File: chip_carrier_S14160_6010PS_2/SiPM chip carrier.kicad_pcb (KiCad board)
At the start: 2 copper layers, 29 x 29 mm, 3 parts, among them J1 Conn_01x10_Socket, J2 Conn_01x10_Socket

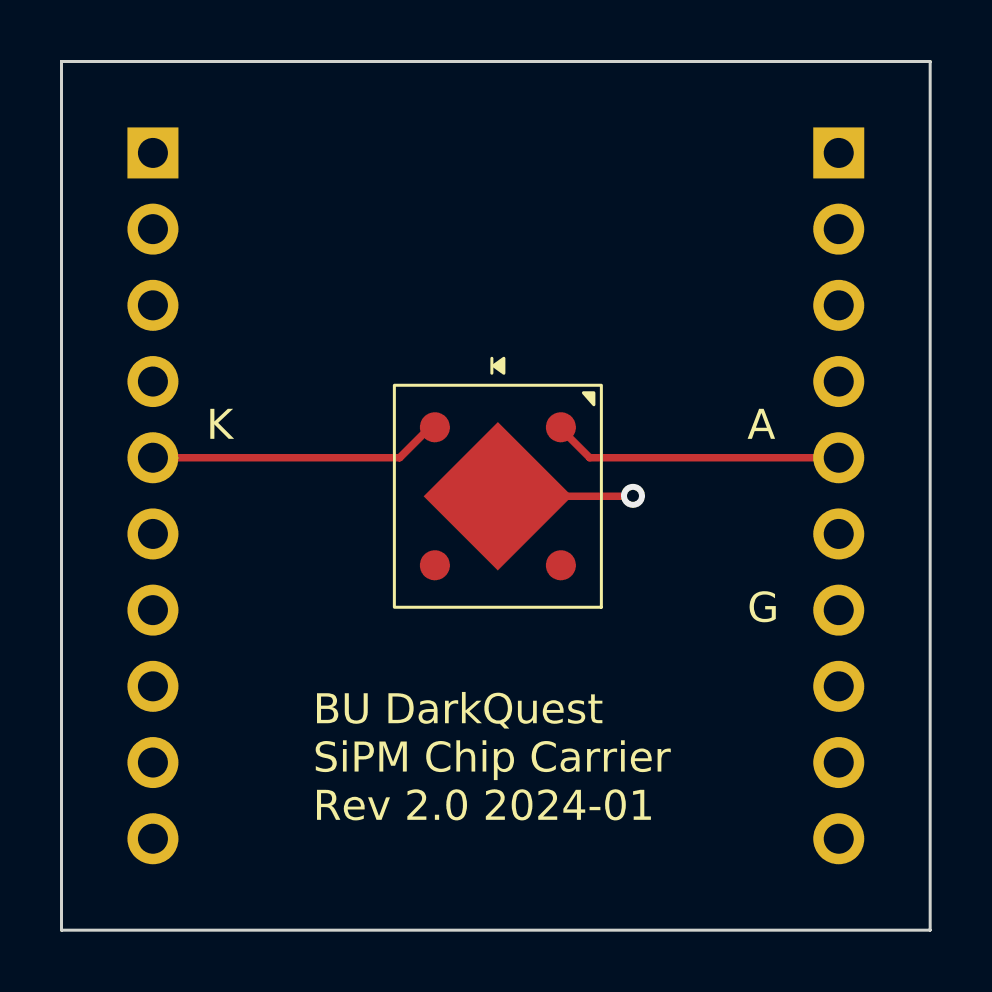
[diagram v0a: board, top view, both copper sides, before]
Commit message: added Rev 8.1: attenuator switch
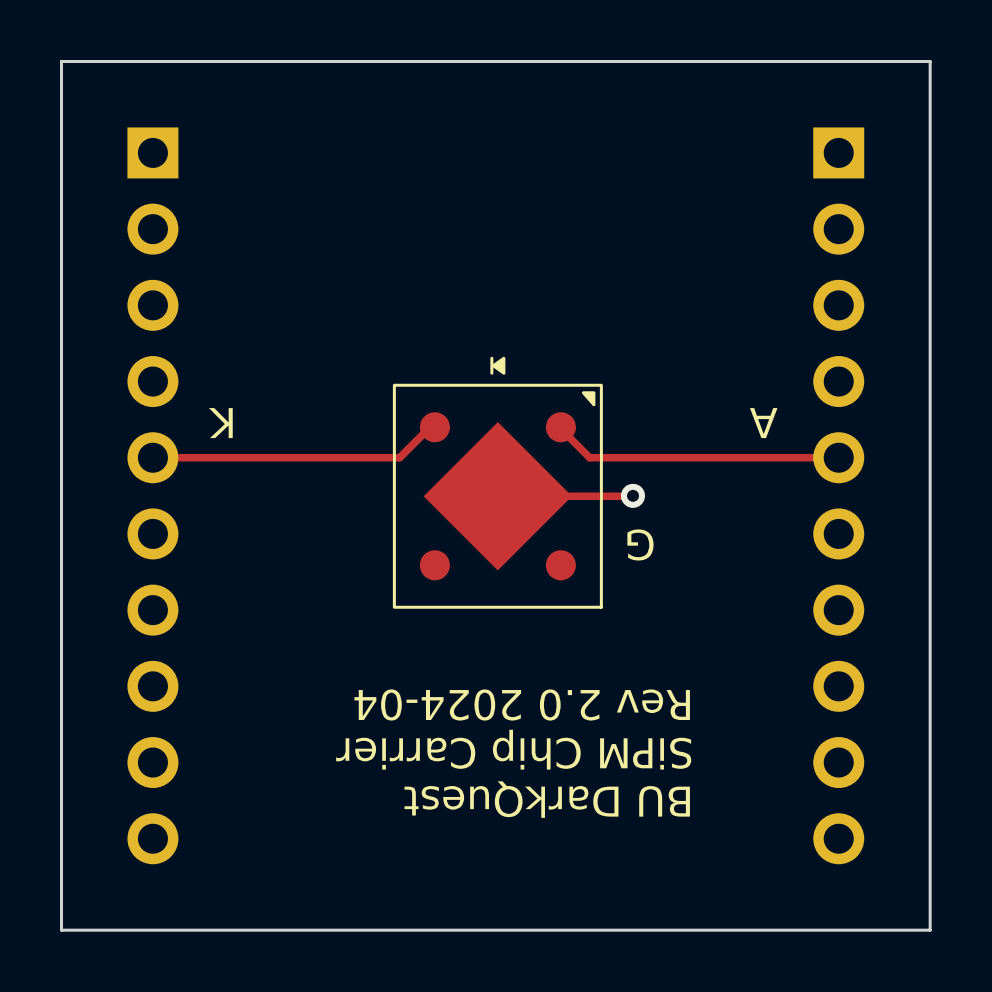
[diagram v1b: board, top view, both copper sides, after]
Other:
- board text added: "BU DarkQuest EMCal Test Stand Chip carrier for Hamamatsu S14160-6010PS 2024-04 ENIG finish"
- board text added: "BU DarkQuest SiPM Chip Carrier Rev 2.0 2024-04"
- board text removed: "BU DarkQuest SiPM Chip Carrier Rev 2.0 2024-01"
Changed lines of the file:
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@@
     (rev "2.0")
     (company "BU DarkQuest EMCal Test Stand")
+    (comment 1 "Finish is ENIG")
   )
   (layers
@@
     (pad_to_mask_clearance 0)
     (pcbplotparams
-      (layerselection 0x00010fc_ffffffff)
+      (layerselection 0x0001ffc_ffffffff)
       (plot_on_all_layers_selection 0x0000000_00000000)
       (disableapertmacros false)
@@
       (drillshape 0)
       (scaleselection 1)
-      (outputdirectory "")
+      (outputdirectory "chipcarrier_2_0")
     )
   )
@@
   (gr_line (start 64.516 35.56) (end 64.516 64.516)
     (stroke (width 0.1) (type default)) (layer "Edge.Cuts"))
-  (gr_text "A" (at 58.42 48.26) (layer "F.SilkS")
-    (effects (font (size 1 1) (thickness 0.15)) (justify left bottom))
-  )
-  (gr_text "G" (at 58.42 54.356) (layer "F.SilkS")
-    (effects (font (size 1 1) (thickness 0.15)) (justify left bottom))
-  )
-  (gr_text "K" (at 40.386 48.26) (layer "F.SilkS")
-    (effects (font (size 1 1) (thickness 0.15)) (justify left bottom))
-  )
-  (gr_text "BU DarkQuest\nSiPM Chip Carrier\nRev 2.0 2024-01" (at 43.942 60.96) (layer "F.SilkS")
-    (effects (font (size 1 1) (thickness 0.15)) (justify left bottom))
-  )
+  (gr_text "A" (at 59.436 46.99 180) (layer "F.SilkS")
+    (effects (font (size 1 1) (thickness 0.15)) (justify left bottom))
+  )
+  (gr_text "G" (at 55.372 51.054 180) (layer "F.SilkS")
+    (effects (font (size 1 1) (thickness 0.15)) (justify left bottom))
+  )
+  (gr_text "K" (at 41.402 46.99 180) (layer "F.SilkS")
+    (effects (font (size 1 1) (thickness 0.15)) (justify left bottom))
+  )
+  (gr_text "BU DarkQuest\nSiPM Chip Carrier\nRev 2.0 2024-04" (at 56.642 56.388 180) (layer "F.SilkS")
+    (effects (font (size 1 1) (thickness 0.15)) (justify left bottom))
+  )
+  (gr_text "BU DarkQuest EMCal Test Stand\nChip carrier for Hamamatsu S14160-6010PS\n2024-04\nENIG finish" (at 71.374 37.592) (layer "Eco1.User")
+    (effects (font (size 1 1) (thickness 0.15)) (justify left bottom))
+  )
